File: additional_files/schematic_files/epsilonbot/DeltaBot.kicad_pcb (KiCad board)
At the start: 2 copper layers, 173.2 x 101.8 mm, 45 parts, among them IC1 ADS1115LIDGSR, J1 USB C PD Modulle, J3 MOTOR_L, J4 MOTOR_R, J5 C1_LIDAR, SW1 SW_SPDT, U1 Radxa_ROCK5B, U2 Buck Converter

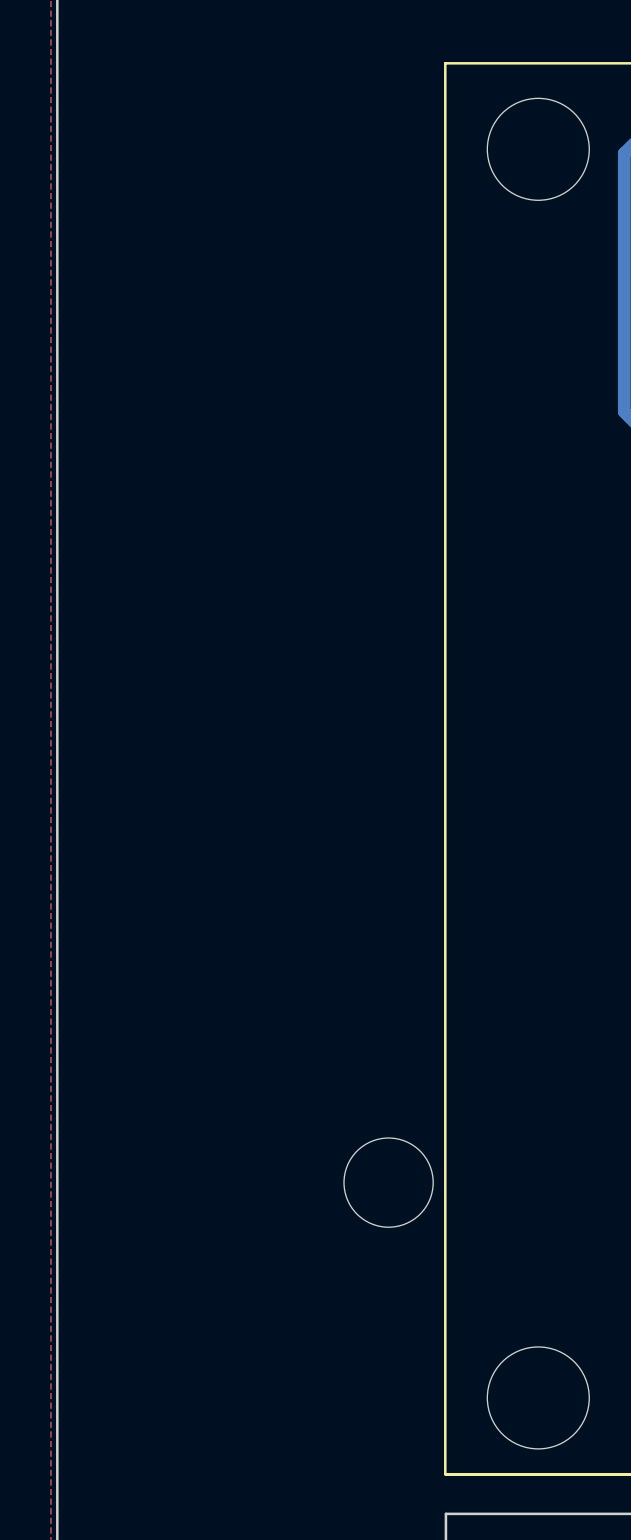
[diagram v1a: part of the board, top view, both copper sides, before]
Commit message: changes to PCB for the ball castor
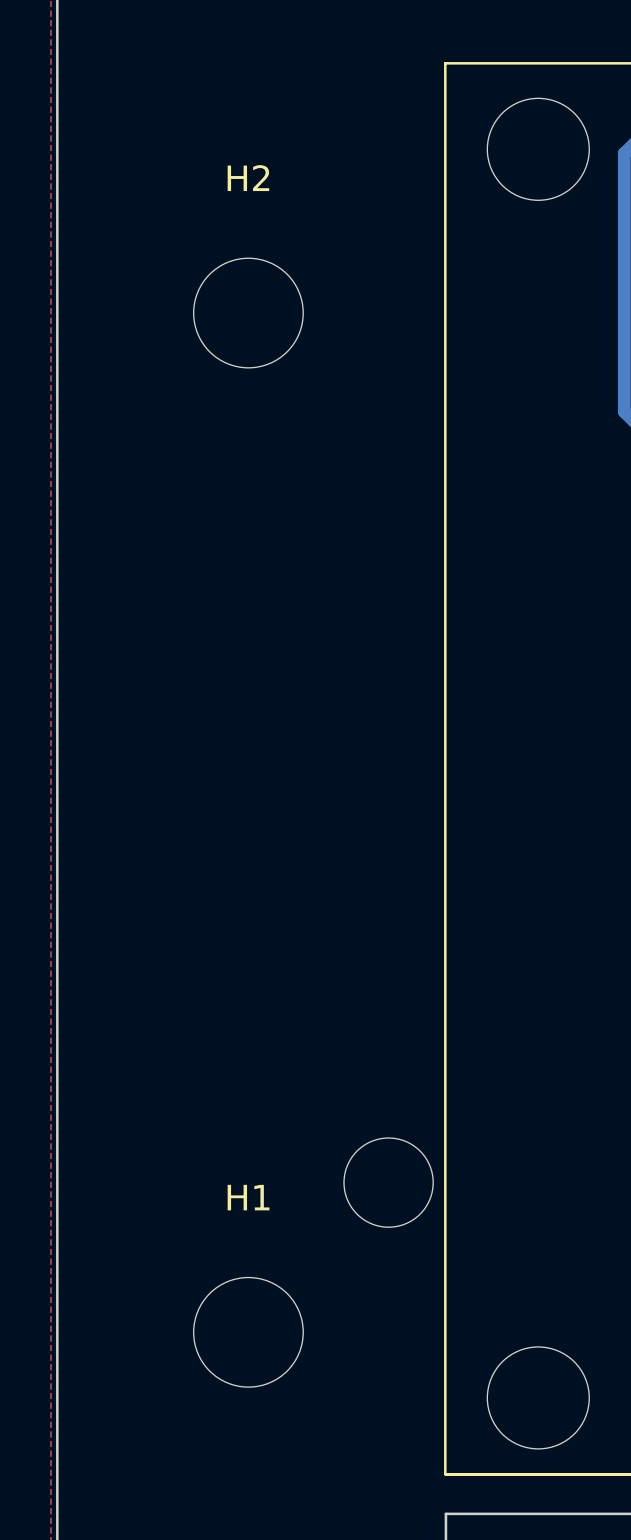
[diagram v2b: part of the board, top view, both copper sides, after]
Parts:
- added H1: MountingHole, MountingHole:MountingHole_4.3mm_M4, F.Cu at (34.2, 119.1)
- added H2: MountingHole, MountingHole:MountingHole_4.3mm_M4, F.Cu at (34.2, 79.1)
- C2: value 1uF -> 10uF
